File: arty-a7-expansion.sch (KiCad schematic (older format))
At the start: 62 parts, among them IC1 TPD8S009DSMR, J2 1140084168, J4 685119134923, J5 UE27AC54100, U1 TPS61232DRCT, U2 MAX3421EEHJ, Y1 ABM8G-12.000MHZ-18-D2Y-T

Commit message: Add revision 2.0.1
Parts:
- removed L1: XFL4020-102MEB, arty-a7-expansion-footprints:XFL4020-102MEB, symbol arty-a7-expansion:XFL4020-102MEB
- added C2, C21, C22, C3, C6, C7, C8: C_100n_0402_16V, arty-a7-expansion-footprints:0402-cap, symbol arty-a7-expansion:C_100n_0402_16V
- added C20, C23, C9: C_10u_0402, arty-a7-expansion-footprints:0402-cap, symbol arty-a7-expansion:C_10u_0402
- added C24, C27, C28: C_1u_0402, arty-a7-expansion-footprints:0402-cap, symbol arty-a7-expansion:C_1u_0402
- added C25, C26: C_3u3_0603, arty-a7-expansion-footprints:0603-cap, symbol arty-a7-expansion:C_3u3_0603
- added C29, C30: C_2n7_0603, arty-a7-expansion-footprints:0603-cap, symbol arty-a7-expansion:C_2n7_0603
- added C31: C_100n_0402_6V3, arty-a7-expansion-footprints:0402-cap, symbol arty-a7-expansion:C_100n_0402_6V3
- added C32, C33: C_180p_0402, arty-a7-expansion-footprints:0402-cap, symbol arty-a7-expansion:C_180p_0402
- added C4, C5: C_4u7_0402, arty-a7-expansion-footprints:0402-cap, symbol arty-a7-expansion:C_4u7_0402
- added D3, D4, D5, D6: LG_L29K-G2J1-24-Z, arty-a7-expansion-footprints:LED_0603, symbol arty-a7-expansion:LG_L29K-G2J1-24-Z
- added FB1, FB2: BLM15AG601SN1D, arty-a7-expansion-footprints:0402-res, symbol arty-a7-expansion:BLM15AG601SN1D
- added IC2: PCA9500PW, arty-a7-expansion-footprints:TSSOP-16, symbol arty-a7-expansion:PCA9500PW
- added J1: SJ-43516-SMT-GR, arty-a7-expansion-footprints:CUI_SJ-43516-SMT-GR, symbol arty-a7-expansion:SJ-43516-SMT-GR
- added J3: SJ-43516-SMT-BE, arty-a7-expansion-footprints:CUI_SJ-43516-SMT-BE, symbol arty-a7-expansion:SJ-43516-SMT-BE
- added JA1: 10883121, arty-a7-expansion-footprints:PinHeader_6x2_P2.54mm_Horizontal_Mirrored, symbol arty-a7-expansion:10883121
- added L1: XFL4020-102MEC, arty-a7-expansion-footprints:XFL4020-102MEB, symbol arty-a7-expansion:XFL4020-102MEC
- added R22, R23: R_1R_0402, arty-a7-expansion-footprints:0402-res, symbol arty-a7-expansion:R_1R_0402
- added R24, R28, R30: R_10k_0402, arty-a7-expansion-footprints:0402-res, symbol arty-a7-expansion:R_10k_0402
- added R25, R26, R27, R39: R_0R_0402, arty-a7-expansion-footprints:0402-res, symbol arty-a7-expansion:R_0R_0402
- added R29, R31, R34, R35: R_5k1_0603, arty-a7-expansion-footprints:0603-res, symbol arty-a7-expansion:R_5k1_0603
- added R32, R33: R_470R_0402, arty-a7-expansion-footprints:0402-res, symbol arty-a7-expansion:R_470R_0402
- added R36, R37: R_2k_0402, arty-a7-expansion-footprints:0402-res, symbol arty-a7-expansion:R_2k_0402
- added R38: R_100k_0402, arty-a7-expansion-footprints:0402-res, symbol arty-a7-expansion:R_100k_0402
- added R40, R41, R42, R43: R_100R_0402, arty-a7-expansion-footprints:0402-res, symbol arty-a7-expansion:R_100R_0402
- added U3: CS4344-CZZ, arty-a7-expansion-footprints:10TSSOP, symbol arty-a7-expansion:CS4344-CZZ
- added U4: CS5343-CZZ, arty-a7-expansion-footprints:10TSSOP, symbol arty-a7-expansion:CS5343-CZZ
- added U5: NC7SZ126P5X, arty-a7-expansion-footprints:SC-70-5, symbol arty-a7-expansion:NC7SZ126P5X
- JB1, JC1, JD1: value 0015912120 -> 10883121; symbol arty-a7-expansion:0015912120 -> arty-a7-expansion:10883121; MPN 0015912120 -> 10883121
- R12: symbol arty-a7-expansion:R_220k_0402 -> arty-a7-expansion:R_220R_0402; MPN CRG0402J220R -> ERJ2GEJ221X; Manufacturer TE_CONNECTIVITY_/_NEOHM -> Panasonic
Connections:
- net labels added: ADIN_LRCK, ADIN_MCLK, ADIN_SCLK, ADIN_SDOUT, ADOUT_LRCK, ADOUT_MCLK, ADOUT_SCLK, ADOUT_SDIN, AINL, AINR, AOUTL, AOUTR, GPIO_SCL, GPIO_SDA, SDOUT
- net labels removed: NC_EN
- wire segments 267 -> 446
- no-connect marks 1 -> 11
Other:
- note added: "Audio converter"
- note added: "GPIO expander"
- note added: "I2C address:\n0x23h - I/O\n0x53h - memory"
- moved on the sheet: C1, C10, C11, C12, C13, C14, C15, C16, C17, C18, C19, D1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

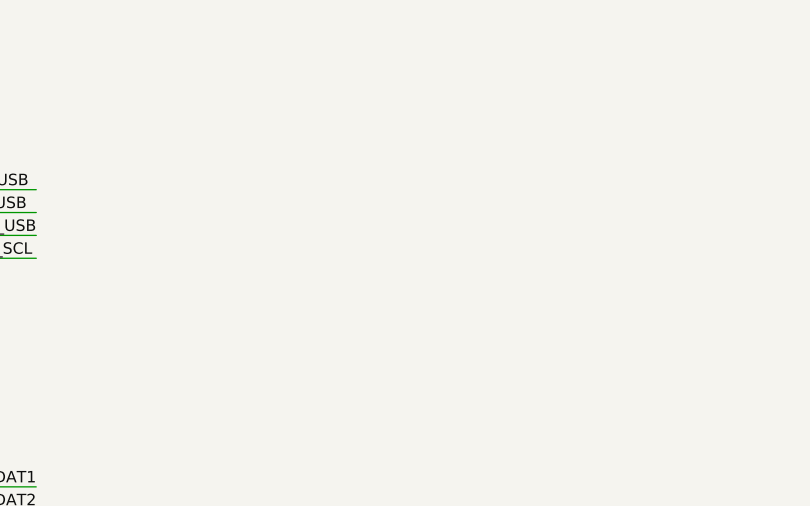
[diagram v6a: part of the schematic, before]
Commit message: Add PWR indicator
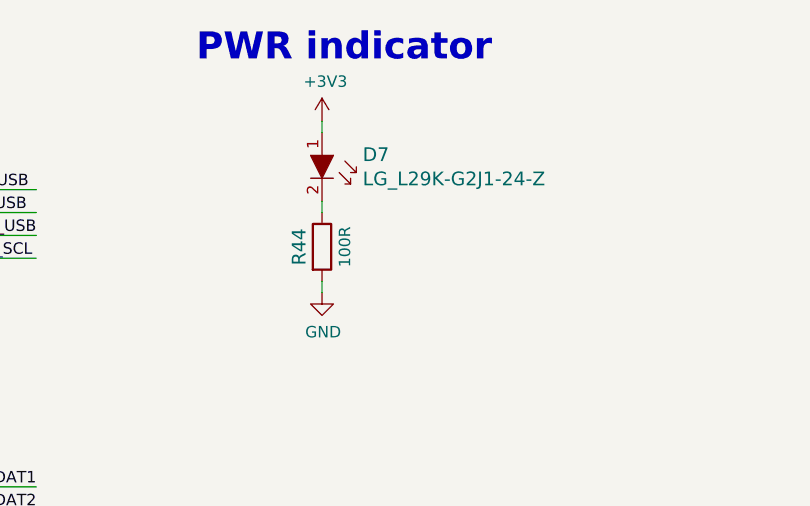
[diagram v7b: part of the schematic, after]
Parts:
- added D7: LG_L29K-G2J1-24-Z, antmicro-footprints:LED_0603, symbol antmicroLEDIndicationDiscrete:LG_L29K-G2J1-24-Z
- added R44: R_100R_0402, arty-a7-expansion-footprints:0402-res, symbol arty-a7-expansion:R_100R_0402
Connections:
- wire segments 446 -> 449
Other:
- note added: "PWR indicator"
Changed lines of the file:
@@
 Connection ~ 2400 7200
 Connection ~ 2400 5600
+$Comp
+L arty-a7-expansion:R_100R_0402 R44
+U 1 1 5FDBB3B2
+P 6900 2200
+F 0 "R44" H 6900 2100 60  0000 C CNN
+F 1 "R_100R_0402" H 6900 2050 60  0001 C CNN
+F 2 "arty-a7-expansion-footprints:0402-res" H 7100 2400 60  0001 L CNN
+F 3 "" H 6900 2200 50  0001 C CNN
+F 4 "BOURNS" H 7100 2600 60  0001 L CNN "Manufacturer"
+F 5 "CR0402-FX-1000GLF" H 7100 2500 60  0001 L CNN "MPN"
+F 6 "100R" H 6900 2300 50  0000 C CNN "Val"
+	1    6900 2200
+	0    1    1    0
+$EndComp
+$Comp
+L antmicroLEDIndicationDiscrete:LG_L29K-G2J1-24-Z D7
+U 1 1 5FCD8625
+P 6900 1900
+F 0 "D7" V 6797 2078 60  0000 L CNN
+F 1 "LG_L29K-G2J1-24-Z" V 6903 2078 60  0000 L CNN
+F 2 "antmicro-footprints:LED_0603" H 7100 2100 60  0001 L CNN
+F 3 "https://dammedia.osram.info/media/resource/hires/osram-dam-2493945/LG%20L29K.pdf" H 7100 2200 60  0001 L CNN
+F 4 "LG L29K-G2J1-24-Z" H 7100 2400 60  0001 L CNN "MPN"
+F 5 "OSRAM Opto Semiconductors Inc." H 7100 3000 60  0001 L CNN "Manufacturer"
+	1    6900 1900
+	0    1    1    0
+$EndComp
+$Comp
+L arty-a7-expansion:GND #PWR0141
+U 1 1 5FD19577
+P 6900 2400
+F 0 "#PWR0141" H 6900 2150 50  0001 C CNN
+F 1 "GND" H 6905 2227 50  0000 C CNN
+F 2 "" H 6900 2400 50  0001 C CNN
+F 3 "" H 6900 2400 50  0001 C CNN
+	1    6900 2400
+	1    0    0    -1
+$EndComp
+$Comp
+L arty-a7-expansion:+3V3 #PWR0142
+U 1 1 601B5E93
+P 6900 1650
+F 0 "#PWR0142" H 6900 1500 50  0001 C CNN
+F 1 "+3V3" H 6915 1823 50  0000 C CNN
+F 2 "" H 6900 1650 50  0001 C CNN
+F 3 "" H 6900 1650 50  0001 C CNN
+	1    6900 1650
+	1    0    0    -1
+$EndComp
+Wire Wire Line
+	6900 1650 6900 1700
+Wire Wire Line
+	6900 2000 6900 2050
+Wire Wire Line
+	6900 2350 6900 2400
+Text Notes 6350 1400 0    118  ~ 24
+PWR indicator
 $EndSCHEMATC

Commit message: Replace micro SD card connector
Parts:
- removed J2: 1140084168, arty-a7-expansion-footprints:MicroSD_1140084168, symbol arty-a7-expansion:1140084168
- added J?: DM3AT-SF-PEJM5, arty-a7-expansion-footprints:MicroSD_DM3AT-SF-PEJM5, symbol arty-a7-expansion:DM3AT-SF-PEJM5
- D7: footprint antmicro-footprints:LED_0603 -> arty-a7-expansion-footprints:LED_0603; symbol antmicroLEDIndicationDiscrete:LG_L29K-G2J1-24-Z -> arty-a7-expansion:LG_L29K-G2J1-24-Z
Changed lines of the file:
@@
 L arty-a7-expansion:GND #PWR0105
 U 1 1 5D761297
-P 17500 12800
-F 0 "#PWR0105" H 17500 12550 50  0001 C CNN
-F 1 "GND" H 17505 12627 50  0000 C CNN
-F 2 "" H 17500 12800 50  0001 C CNN
-F 3 "" H 17500 12800 50  0001 C CNN
-	1    17500 12800
+P 18350 12900
+F 0 "#PWR0105" H 18350 12650 50  0001 C CNN
+F 1 "GND" H 18355 12727 50  0000 C CNN
+F 2 "" H 18350 12900 50  0001 C CNN
+F 3 "" H 18350 12900 50  0001 C CNN
+	1    18350 12900
 	1    0    0    -1
 $EndComp
@@
 	4700 3750 4550 3750
 $Comp
-L arty-a7-expansion:1140084168 J2
-U 1 1 5D7B2684
-P 17150 11900
-F 0 "J2" H 16800 12650 50  0000 C CNN
-F 1 "1140084168" H 16975 12500 50  0000 C CNN
-F 2 "arty-a7-expansion-footprints:MicroSD_1140084168" H 17050 11250 50  0001 C CNN
-F 3 "" H 16800 11900 50  0001 C CNN
-F 4 "1140084168" H 16975 12625 50  0001 C CNN "MPN"
-F 5 "Amphenol" H 16925 12575 50  0000 C CNN "Manufacturer"
-	1    17150 11900
-	1    0    0    -1
-$EndComp
-$Comp
 L arty-a7-expansion:C_100n_0402_6V3 C1
 U 1 1 5D7BA763
@@
 CD
 Wire Wire Line
-	17500 12250 17500 12800
+	18350 12350 18350 12900
 Wire Wire Line
 	16650 12350 16550 12350
@@
 $EndComp
 $Comp
-L antmicroLEDIndicationDiscrete:LG_L29K-G2J1-24-Z D7
+L arty-a7-expansion:LG_L29K-G2J1-24-Z D7
 U 1 1 5FCD8625
 P 6900 1900
 F 0 "D7" V 6797 2078 60  0000 L CNN
 F 1 "LG_L29K-G2J1-24-Z" V 6903 2078 60  0000 L CNN
-F 2 "antmicro-footprints:LED_0603" H 7100 2100 60  0001 L CNN
+F 2 "arty-a7-expansion-footprints:LED_0603" H 7100 2100 60  0001 L CNN
 F 3 "https://dammedia.osram.info/media/resource/hires/osram-dam-2493945/LG%20L29K.pdf" H 7100 2200 60  0001 L CNN
 F 4 "LG L29K-G2J1-24-Z" H 7100 2400 60  0001 L CNN "MPN"
@@
 Text Notes 6350 1400 0    118  ~ 24
 PWR indicator
+$Comp
+L arty-a7-expansion:DM3AT-SF-PEJM5 J?
+U 1 1 6112B8A7
+P 17550 11850
+F 0 "J?" H 17500 12849 50  0000 C CNN
+F 1 "DM3AT-SF-PEJM5" H 17500 12758 50  0000 C CNN
+F 2 "arty-a7-expansion-footprints:MicroSD_DM3AT-SF-PEJM5" H 17550 11850 50  0001 C CNN
+F 3 "" H 17550 11850 50  0001 C CNN
+F 4 "HIROSE" H 17500 12667 50  0000 C CNN "Manufacturer"
+F 5 "DM3AT-SF-PEJM5" H 17500 12576 50  0000 C CNN "MPN"
+	1    17550 11850
+	1    0    0    -1
+$EndComp
 $EndSCHEMATC
